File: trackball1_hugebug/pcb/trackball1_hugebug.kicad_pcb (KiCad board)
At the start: 2 copper layers, 61.9 x 44.5 mm, 18 parts, among them J1 Conn_01x03, J10 Conn_01x03, J11 Conn_01x03, J2 Conn_01x03, J3 Conn_01x03, J4 Conn_01x03, J5 Conn_01x08, J6 Conn_01x02, J7 Conn_01x02, J8 Conn_01x03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

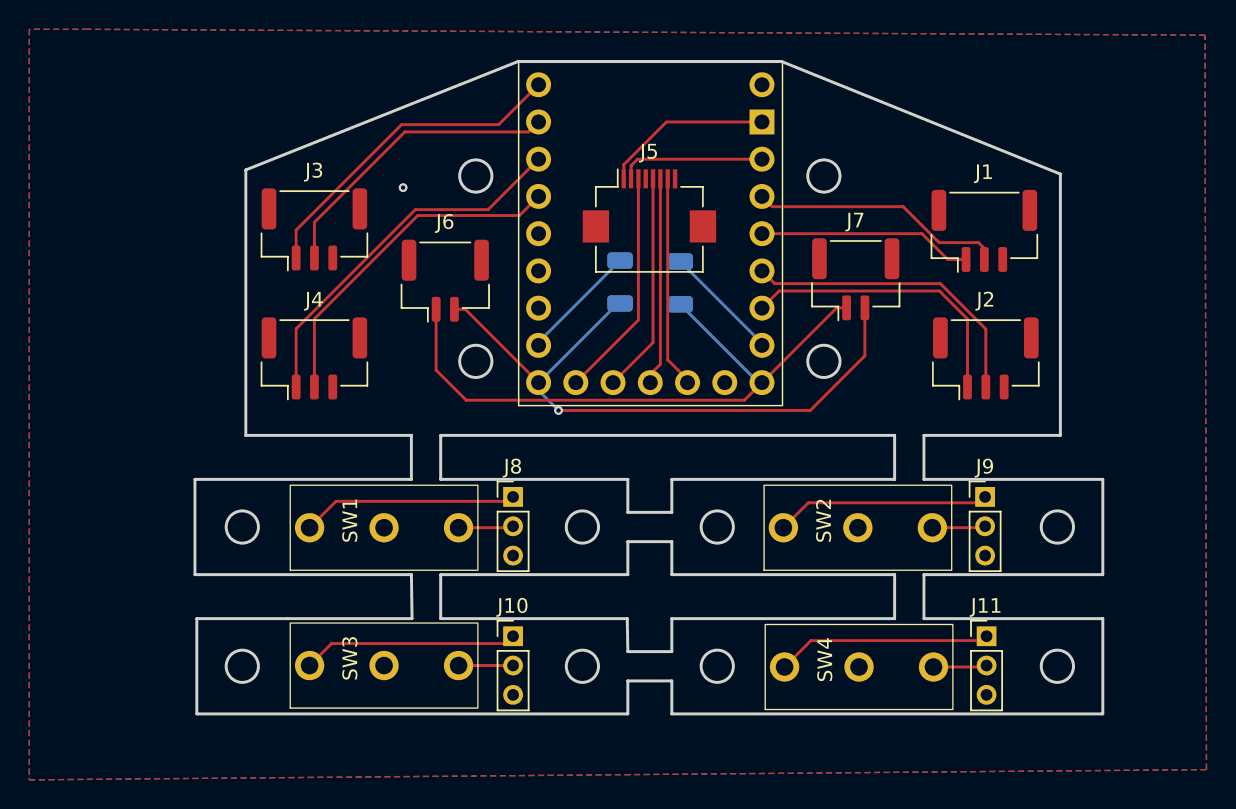
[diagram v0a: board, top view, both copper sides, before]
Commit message: refactor: increase footprint pads for easier soldering
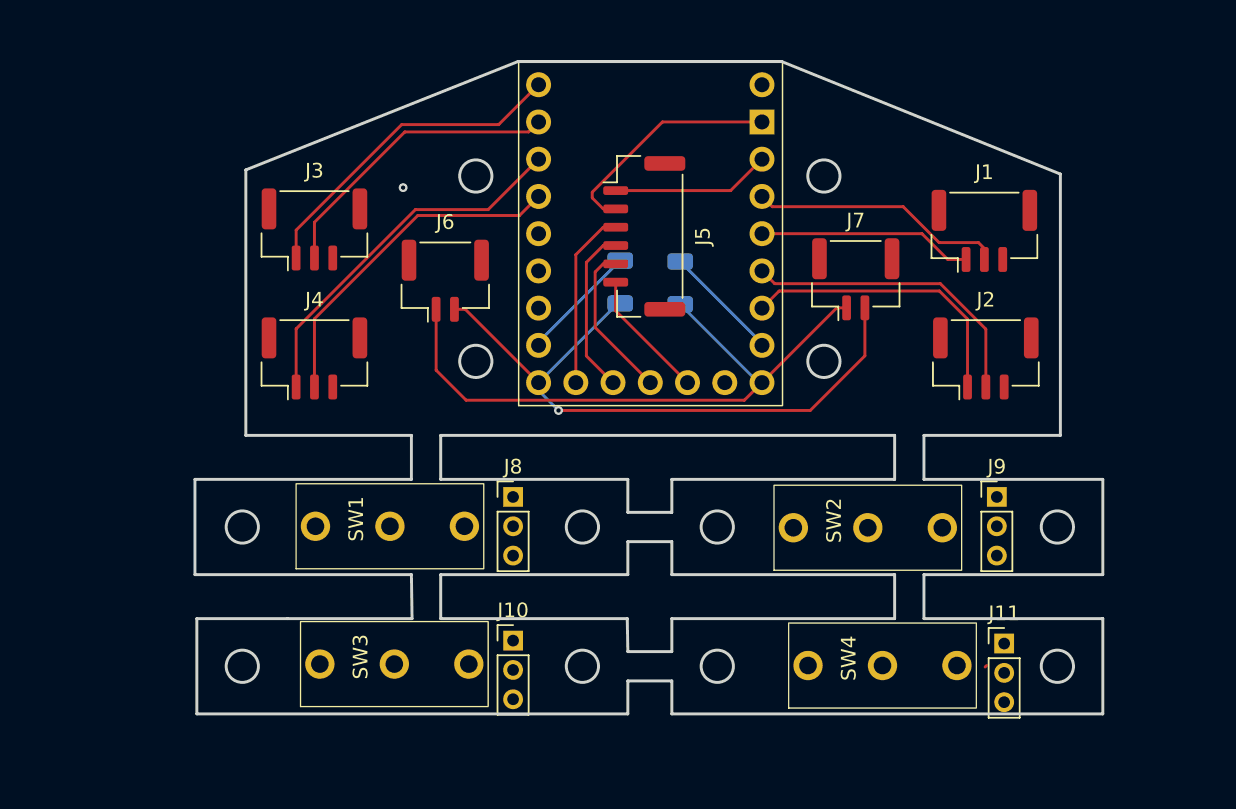
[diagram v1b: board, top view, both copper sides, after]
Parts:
- J5: value Conn_01x08 -> Conn_01x06; footprint Connector_FFC-FPC:Hirose_FH12-8S-0.5SH_1x08-1MP_P0.50mm_Horizontal -> Connector_JST:JST_GH_BM06B-GHS-TBT_1x06-1MP_P1.25mm_Vertical
- SW1, SW2, SW3, SW4: value SW_SPDT -> SW_SPDT_312
- moved J5 2.10 mm to (161.8, 84.1), turned to -90 degrees
- moved SW4 1.60 mm to (178.1, 113.4)
- moved J11 1.30 mm to (186.4, 111.9)
- moved J9 0.80 mm to (185.9, 101.9)
- moved SW3 0.71 mm to (144.8, 113.3)
- moved SW2 0.68 mm to (177.1, 104.0)
- moved SW1 0.41 mm to (144.5, 103.9)
- moved J10 0.30 mm to (152.9, 111.7)
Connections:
- J1 pad 2: btn1 -> GND
- J1 pad 3: GND -> btn1
- J10 pad 3: GND -> Net-(J10-Pin_3)
- J11 pad 3: GND -> Net-(J11-Pin_3)
- J2 pad 2: btn2 -> GND
- J2 pad 3: GND -> btn2
- J3 pad 2: btn3 -> GND
- J3 pad 3: GND -> btn3
- J4 pad 2: btn4 -> GND
- J4 pad 3: GND -> btn4
- J5 pad 1: GND -> VIN
- J5 pad 2: VIN -> GND
- J5 pad 4: unconnected-(J5-Pin_4-Pad4) -> SDIO
- J5 pad 5: SDIO -> SCLK
- J5 pad 6: SCLK -> MOTION
- J8 pad 3: GND -> Net-(J8-Pin_3)
- J9 pad 3: GND -> Net-(J9-Pin_3)
- SW1 pad 2: GND -> Net-(J8-Pin_2)
- SW1 pad 3: Net-(J8-Pin_2) -> Net-(J8-Pin_3)
- SW2 pad 2: GND -> Net-(J9-Pin_2)
- SW2 pad 3: Net-(J9-Pin_2) -> Net-(J9-Pin_3)
- SW3 pad 2: GND -> Net-(J10-Pin_2)
- SW3 pad 3: Net-(J10-Pin_2) -> Net-(J10-Pin_3)
- SW4 pad 2: GND -> Net-(J11-Pin_2)
- SW4 pad 3: Net-(J11-Pin_2) -> Net-(J11-Pin_3)
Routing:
- net Net-(J8-Pin_1): track 14.7 -> 0.00 mm
- net Net-(J11-Pin_1): track 14.6 -> 0.00 mm
- net Net-(J9-Pin_1): track 14.6 -> 0.00 mm
- net Net-(J10-Pin_1): track 14.5 -> 0.00 mm
- net MOTION: track 14.5 -> 8.88 mm
- net GND: track 11.6 -> 15.9 mm
- net Net-(J10-Pin_2): track 3.89 -> 0.00 mm
- net Net-(J8-Pin_2): track 3.76 -> 0.14 mm
- net SDIO: track 15.0 -> 11.4 mm
- net Net-(J9-Pin_2): track 3.60 -> 0.00 mm
- net Net-(J11-Pin_2): track 3.66 -> 0.14 mm
- net SCLK: track 14.2 -> 10.7 mm
- net nCS: track 15.7 -> 12.2 mm
- net VIN: track 10.0 -> 10.9 mm
- removed copper zone on B.Cu, net GND
- removed copper zone on F.Cu, net GND
